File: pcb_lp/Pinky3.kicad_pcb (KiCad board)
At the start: 2 copper layers, 137 x 100.9 mm, 97 parts, among them P1 i2c-pin, P2 i2c-pin, SW1 RESET_SW, SW10 SW_PUSH, SW11 SW_PUSH, SW12 SW_PUSH, SW13 SW_PUSH, SW14 SW_PUSH, SW15 SW_PUSH, SW16 SW_PUSH, SW17 SW_PUSH, SW18 SW_PUSH, SW19 SW_PUSH, SW2 SW_PUSH, SW20 SW_PUSH, SW21 SW_PUSH, SW22 SW_PUSH, SW23 SW_PUSH, SW24 SW_PUSH, SW25 SW_PUSH, SW26 SW_PUSH, SW3 SW_PUSH, SW4 SW_PUSH, SW5 SW_PUSH, SW6 SW_PUSH, SW7 SW_PUSH, SW8 SW_PUSH, SW9 SW_PUSH, U1 ProMicro

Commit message: reroute for batt and add legend
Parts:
- moved G*** 10.1 mm to (63.9, 125.3)
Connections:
- REF** pad 1: GND -> battery+
- REF** pad 2: battery+ -> GND
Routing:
- net battery+: track 96.6 -> 100.1 mm
- net GND: track 237.5 -> 238.0 mm
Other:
- board text added: "batt"
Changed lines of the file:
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@@
 	(footprint "lib:pinky3"
 		(layer "F.Cu")
-		(at 53.9 124.7)
+		(at 63.937473 125.343492)
 		(property "Reference" "G***"
 			(at 0 0 0)
@@
 			(layers "B.Cu" "B.Paste" "B.Mask")
 			(roundrect_rratio 0.25)
-			(net 29 "GND")
+			(net 48 "battery+")
 		)
 		(pad "2" smd roundrect
@@
 			(layers "B.Cu" "B.Paste" "B.Mask")
 			(roundrect_rratio 0.25)
-			(net 48 "battery+")
+			(net 29 "GND")
 		)
 		(pad "MP" smd roundrect
@@
 		(layer "Edge.Cuts")
 	)
+	(gr_text "batt"
+		(at 42.708661 130.437367 90)
+		(layer "F.Cu")
+		(effects
+			(font
+				(size 1 1)
+				(thickness 0.25)
+				(bold yes)
+			)
+			(justify left bottom)
+		)
+	)
+	(gr_text "batt"
+		(at 42.866565 120.884181 90)
+		(layer "B.Cu")
+		(effects
+			(font
+				(size 1 1)
+				(thickness 0.25)
+				(bold yes)
+			)
+			(justify left bottom mirror)
+		)
+	)
 	(gr_text "ver. 1.0\ndesigned by @tamanishi"
 		(at 45.5 128.2 0)
@@
 		(start 76.99736 128.925)
 		(end 77.679586 128.242774)
-		(width 0.5)
+		(width 0.25)
 		(layer "F.Cu")
 		(net 29)
@@
 		(start 77.679586 128.242774)
 		(end 78.557226 128.242774)
-		(width 0.5)
+		(width 0.25)
 		(layer "F.Cu")
 		(net 29)
@@
 		(start 74.720414 128.242774)
 		(end 75.40264 128.925)
-		(width 0.5)
+		(width 0.25)
 		(layer "F.Cu")
 		(net 29)
@@
 		(start 75.40264 128.925)
 		(end 76.99736 128.925)
-		(width 0.5)
+		(width 0.25)
 		(layer "F.Cu")
 		(net 29)
@@
 		(start 50.157313 128.242774)
 		(end 74.720414 128.242774)
-		(width 0.5)
+		(width 0.25)
 		(layer "F.Cu")
 		(net 29)
@@
 	)
 	(segment
+		(start 43.508886 126.377214)
+		(end 42.268059 126.377214)
+		(width 0.25)
+		(layer "B.Cu")
+		(net 29)
+	)
+	(segment
 		(start 82.512597 133.109596)
 		(end 82.108323 132.705322)
@@
 	)
 	(segment
-		(start 82.512597 134.242025)
-		(end 82.512597 133.109596)
+		(start 44.744557 125.141543)
+		(end 43.508886 126.377214)
 		(width 0.25)
 		(layer "B.Cu")
@@
 	)
 	(segment
-		(start 44.744557 125.141543)
-		(end 42.282388 125.141543)
+		(start 82.512597 134.242025)
+		(end 82.512597 133.109596)
 		(width 0.25)
 		(layer "B.Cu")
@@
 	)
 	(segment
+		(start 45.494557 125.452204)
+		(end 45.494557 124.830882)
+		(width 0.5)
+		(layer "B.Cu")
+		(net 48)
+	)
+	(segment
+		(start 44.556349 126.390412)
+		(end 45.494557 125.452204)
+		(width 0.5)
+		(layer "B.Cu")
+		(net 48)
+	)
+	(segment
+		(start 44.495594 126.390412)
+		(end 44.556349 126.390412)
+		(width 0.5)
+		(layer "B.Cu")
+		(net 48)
+	)
+	(segment
 		(start 79.124702 132.099236)
 		(end 79.124702 132.697182)
@@
 	)
 	(segment
+		(start 45.055218 124.391543)
+		(end 43.00373 124.391543)
+		(width 0.5)
+		(layer "B.Cu")
+		(net 48)
+	)
+	(segment
 		(start 47.897258 130.185429)
 		(end 47.897258 130.789691)
@@
 	)
 	(segment
-		(start 47.462558 131.224391)
-		(end 47.897258 130.789691)
-		(width 0.25)
+		(start 45.494557 124.830882)
+		(end 45.055218 124.391543)
+		(width 0.5)
 		(layer "B.Cu")
 		(net 48)
 	)
 	(segment
-		(start 44.495594 126.390412)
-		(end 42.281257 126.390412)
-		(width 0.5)
+		(start 47.462558 131.224391)
+		(end 47.897258 130.789691)
+		(width 0.25)
 		(layer "B.Cu")
 		(net 48)
@@
 		(layer "B.Cu")
 		(net 48)
+	)
+	(segment
+		(start 43.00373 124.391543)
+		(end 42.268059 125.127214)
+		(width 0.5)
+		(layer "B.Cu")
+		(net 48)

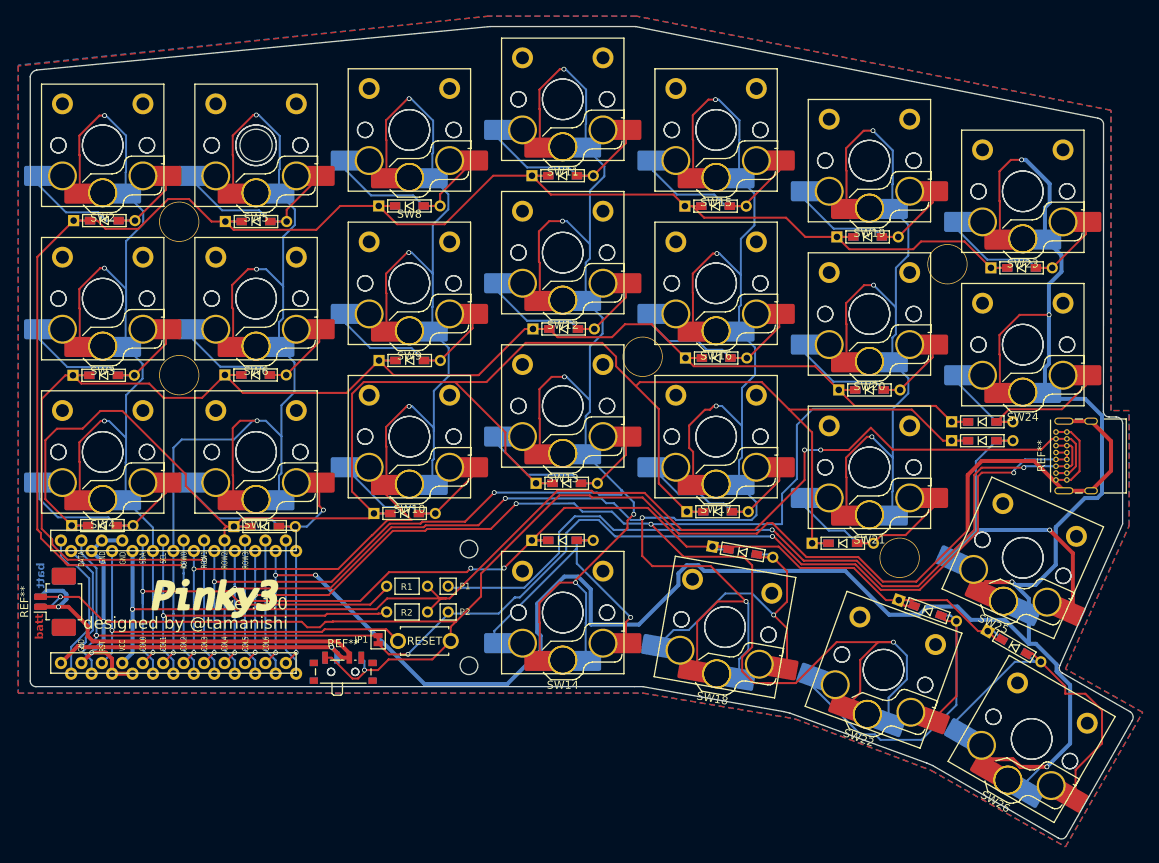
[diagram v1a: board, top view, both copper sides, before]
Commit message: update lp version for pcb, switchplate, bottom-plate
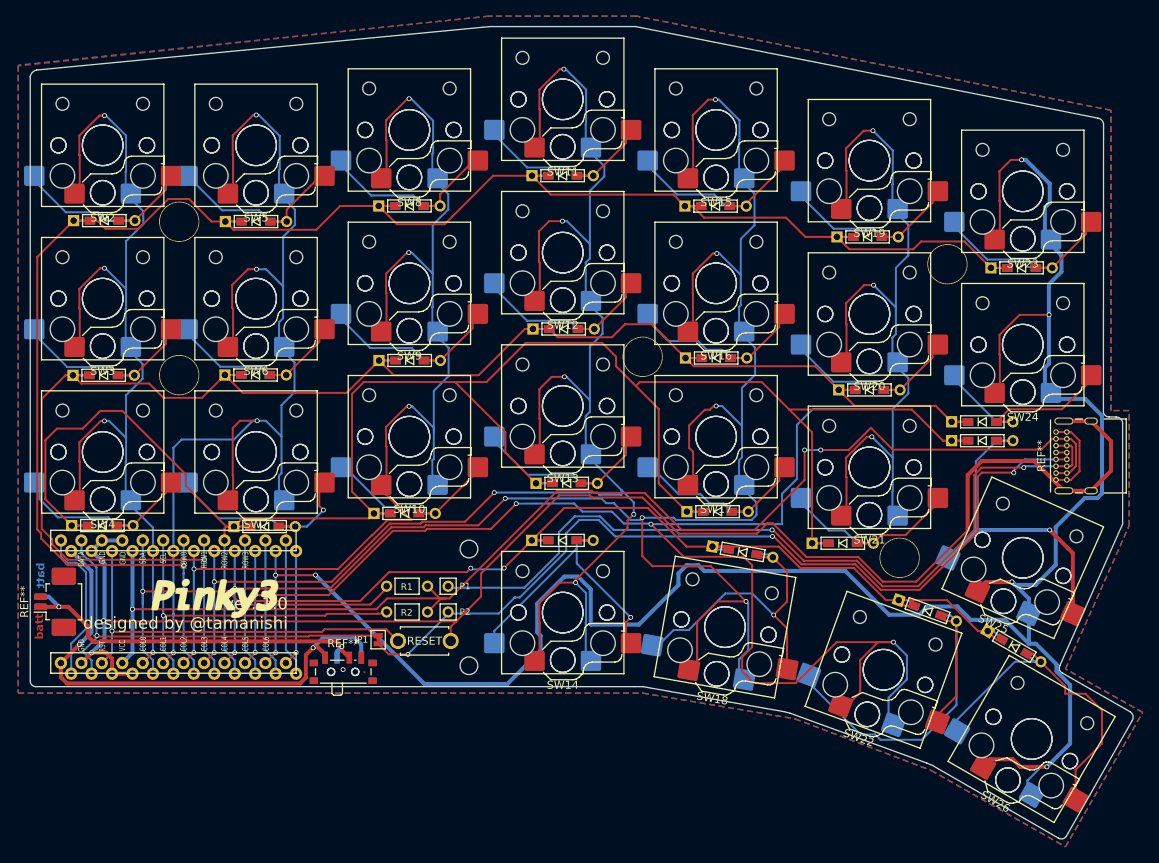
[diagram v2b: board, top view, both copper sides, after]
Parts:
- removed ?: , 
- SW10, SW11, SW12, SW13, SW14 (x2), SW15, SW16, SW17, SW18 (x2), SW19, SW2 (x2), SW20, SW21, SW22 (x2), SW23, SW24, SW25 (x2), SW26 (x2), SW3, SW4, SW5 (x20), SW6, SW7, SW8, SW9: footprint Switch_Keyboard_Hotswap_Kailh:SW_Hotswap_Kailh_Choc_V1V2_Plated_1.00u -> Switch_Keyboard_Hotswap_Kailh:SW_Hotswap_Kailh_Choc_V1V2_1.00u
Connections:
- REF** pad 1: battery+ -> battery_in (x2)
- REF** pad : battery+ -> battery_in
- REF** pad 1: GND -> battery_out (x2)
- REF** pad 2: battery+ -> battery_in
- SW26 pad 2: Net-(D25-Pad2) -> (no net) (x2)
- U1 pad 24: battery+ -> battery_out
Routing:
- net battery+: track 100.1 -> 0.00 mm, vias 3 -> 0
- net battery_out: track 0.00 -> 64.6 mm, vias 0 -> 2
- net battery_in: track 0.00 -> 47.1 mm, vias 0 -> 2
- net GND: track 238.0 -> 205.4 mm, vias 4 -> 3
